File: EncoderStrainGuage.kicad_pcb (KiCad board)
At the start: 2 copper layers, 90.6 x 37.4 mm, 60 parts, among them IC1 LM60CIM3_NOPB, J1 Conn_01x05, J2 MM8130-2600RA2, J3 MM8130-2600RA2, J4 Rotary Encoder, J5 Conn_01x02_Male, J6 Conn_01x02_Male, U1 PIC16LF88-I_SO, U2 OPAMP, U3 CC2570RHAT, U4 AP3428KTTR, Y1 Crystal_GND24, Y2 Crystal

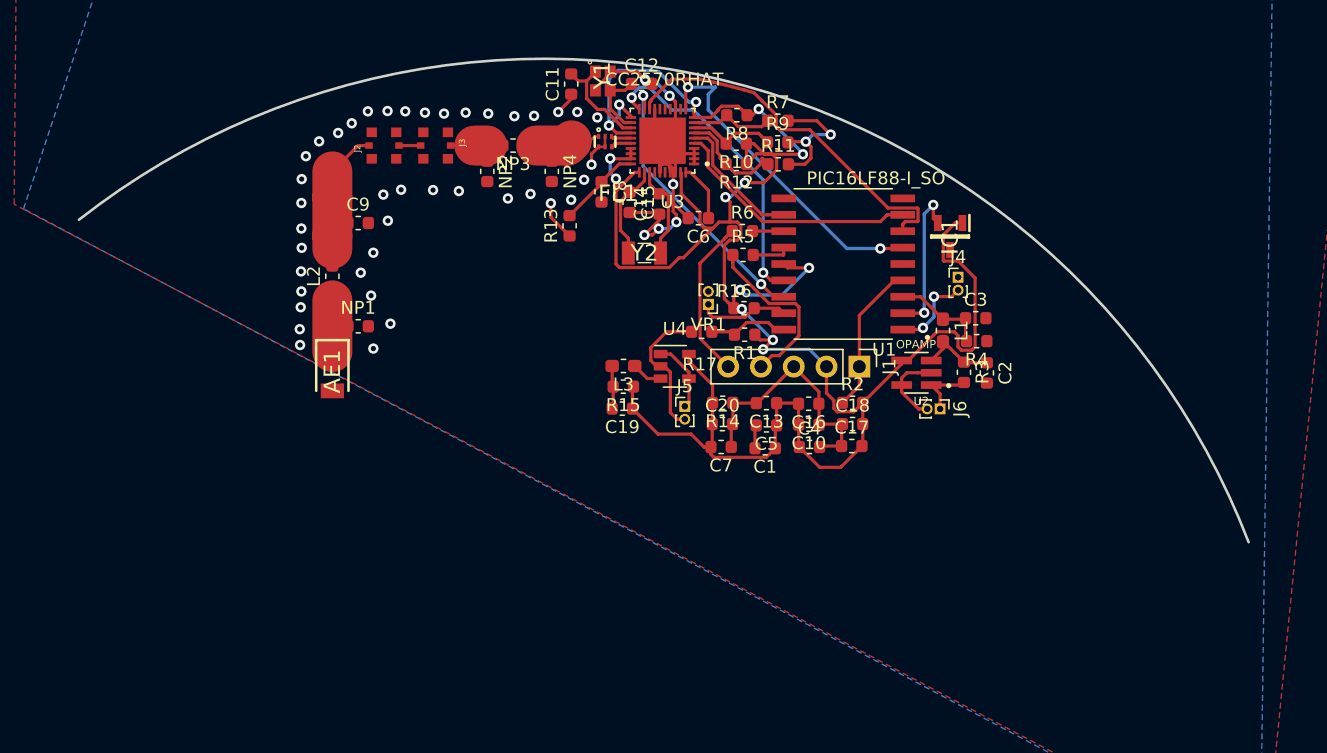
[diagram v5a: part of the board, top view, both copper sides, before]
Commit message: cleaned up a few routes
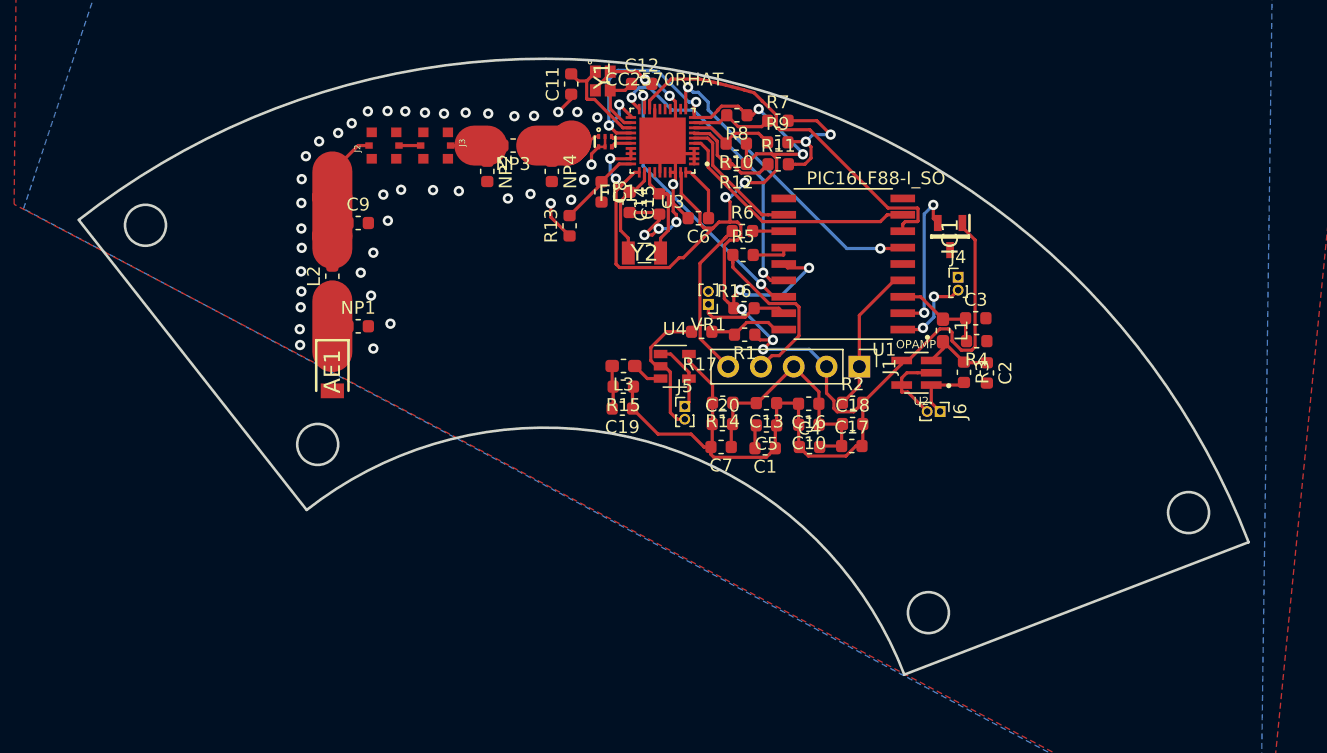
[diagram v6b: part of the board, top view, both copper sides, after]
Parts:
- moved J6 0.20 mm to (212.6, -3.40)
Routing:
- net +3V3: track 178.0 -> 172.8 mm
- net GND: track 98.8 -> 95.4 mm
- net RTS: track 25.4 -> 24.0 mm
- net Net-(R11-Pad1): track 8.51 -> 7.92 mm
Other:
- board size 90.6 x 37.4 mm -> 90.6 x 47.7 mm

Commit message: SD Card
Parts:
- added C21: 100n, Capacitor_SMD:C_0603_1608Metric, F.Cu at (157.9, 99.7)
- added C22: 100n, Capacitor_SMD:C_0603_1608Metric, F.Cu at (161.3, 95.6)
- added C23: .1uF, Capacitor_SMD:C_0603_1608Metric, F.Cu at (162.0, 98.1)
- added C24: 1uF, Capacitor_SMD:C_0603_1608Metric, F.Cu at (165.3, 95.6)
- added C25: 330P, Capacitor_SMD:C_0603_1608Metric, F.Cu at (128.7, 98.1)
- added C26: NP, Capacitor_SMD:C_0603_1608Metric, F.Cu at (132.7, 98.1)
- added C27: 330P, Capacitor_SMD:C_0603_1608Metric, F.Cu at (128.7, 100.7)
- added C28: NP, Capacitor_SMD:C_0603_1608Metric, F.Cu at (140.8, 96.2)
- added C29: 100n, Capacitor_SMD:C_0603_1608Metric, F.Cu at (132.7, 100.7)
- added C30: 1n, Capacitor_SMD:C_0603_1608Metric, F.Cu at (136.7, 98.1)
- added C31: 330P, Capacitor_SMD:C_0603_1608Metric, F.Cu at (145.6, 90.1)
- added C32: NP, Capacitor_SMD:C_0603_1608Metric, F.Cu at (140.7, 98.7)
- added J7: 47219-2001, DFFP-master:SD_472192001, F.Cu at (97.4, 94.6)
- added L4: 0, Inductor_SMD:L_0603_1608Metric_Pad1.05x0.95mm_HandSolder, F.Cu at (115.6, 89.3)
- added L5: 0, Inductor_SMD:L_0603_1608Metric_Pad1.05x0.95mm_HandSolder, F.Cu at (115.6, 91.9)
- added L6: 0, Inductor_SMD:L_0603_1608Metric_Pad1.05x0.95mm_HandSolder, F.Cu at (120.0, 89.3)
- added R1: 470, Resistor_SMD:R_0603_1608Metric, F.Cu at (145.6, 92.6)
- added R16: 470, Resistor_SMD:R_0603_1608Metric, F.Cu at (136.7, 100.7)
- added R17: 470, Resistor_SMD:R_0603_1608Metric, F.Cu at (144.8, 96.2)
- added RV1: 500 TRIM, DFFP-master:TRIM_3314J-1-202E, F.Cu at (129.7, 92.6)
- added RV2: 500 TRIM, DFFP-master:TRIM_3314J-1-202E, F.Cu at (135.8, 92.6)
- added RV3: 10k TRIM, DFFP-master:TC33X-2_1, F.Cu at (141.2, 91.7)
- added U5: INA333AIDGKR, DFFP-master:INA333AIDGKR, F.Cu at (136.1, 80.7)
- added VR2: StrainG 350 ohm, Connector_PinHeader_1.00mm:PinHeader_1x02_P1.00mm_Vertical, F.Cu at (157.6, 95.9)
- VR1: value StrainGuage -> StrainG 350 ohm
- moved AE1 147.0 mm to (119.4, 133.1)
- moved C1 147.0 mm to (152.9, 139.0)
- moved C10 147.0 mm to (156.3, 137.2)
- moved C12 147.0 mm to (143.4, 110.8)
- moved C13 147.0 mm to (153.0, 135.5)
- moved C14 147.0 mm to (144.7, 120.1)
- moved C15 147.0 mm to (142.4, 120.0)
- moved C16 147.0 mm to (156.3, 135.6)
- moved C18 147.0 mm to (159.7, 137.1)
- moved C19 147.0 mm to (141.9, 135.9)
- moved C20 147.0 mm to (149.6, 137.1)
- moved C3 147.0 mm to (169.3, 128.9)
- moved C4 147.0 mm to (156.4, 138.9)
- moved C7 147.0 mm to (149.5, 138.9)
- moved C8 147.0 mm to (140.3, 119.1)
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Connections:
- U1 pad 10: Net-(U1-Pad10) -> SCK
- U1 pad 17: Str2 -> Net-(U1-Pad17)
- VR1 pad 1: Str2 -> Str+

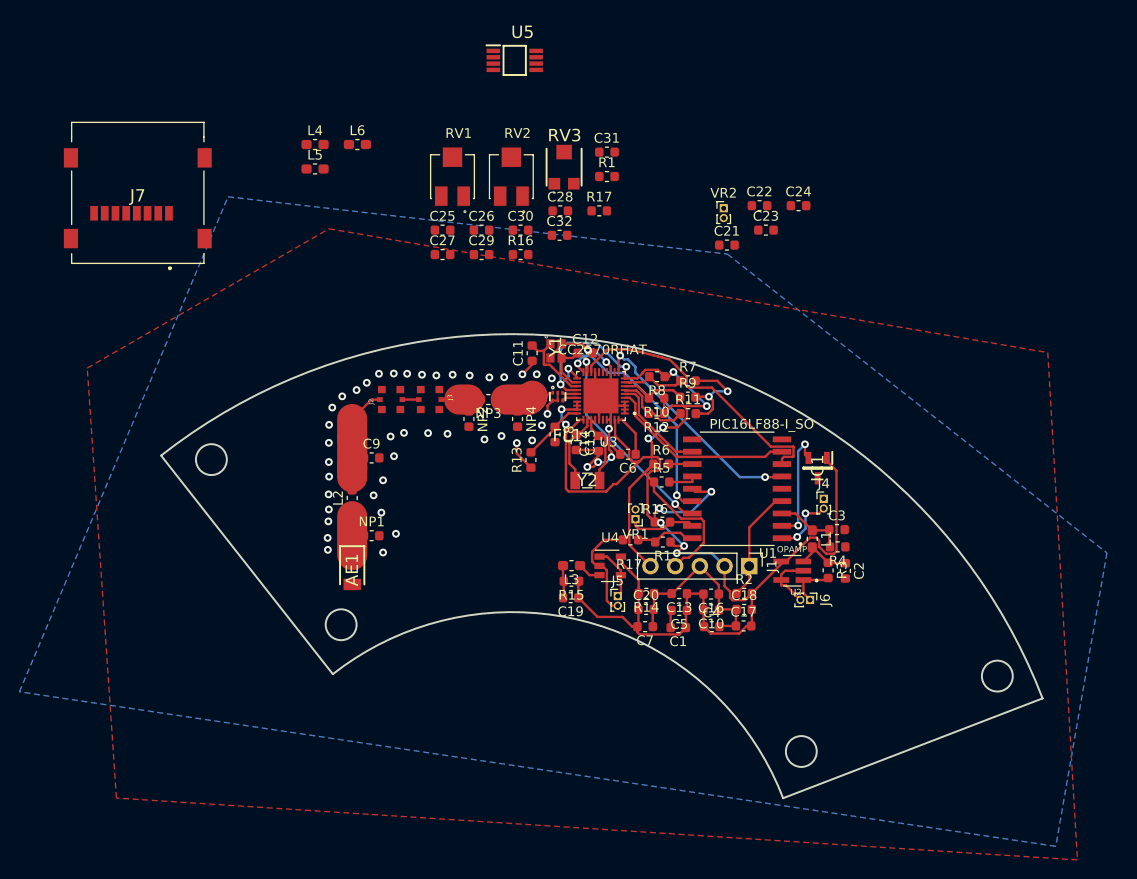
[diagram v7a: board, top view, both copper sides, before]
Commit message: "Fixed all routing"
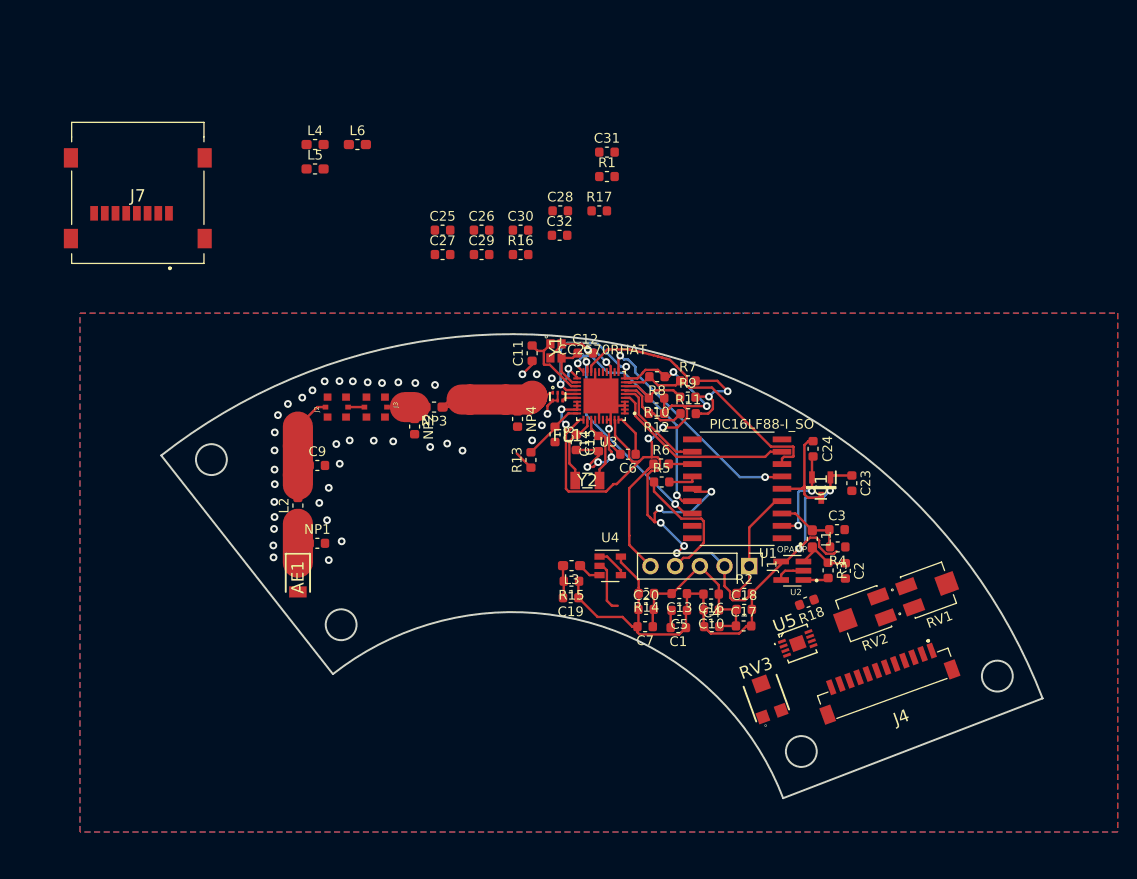
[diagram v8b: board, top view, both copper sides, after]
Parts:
- removed C21, C22: 100n, Capacitor_SMD:C_0603_1608Metric
- removed J5, J6: Conn_01x02_Male, Connector_PinHeader_1.00mm:PinHeader_1x02_P1.00mm_Vertical
- removed the R1 at (151.4, 130.2)
- removed the R16 at (151.3, 128.2)
- removed the R17 at (148.0, 130.0)
- removed VR1, VR2: StrainG 350 ohm, Connector_PinHeader_1.00mm:PinHeader_1x02_P1.00mm_Vertical
- added R18: 200k, Resistor_SMD:R_0603_1608Metric, F.Cu at (166.2, 136.4)
- J4: value Rotary Encoder -> Conn_01x12; footprint Connector_PinHeader_1.00mm:PinHeader_1x02_P1.00mm_Vertical -> DFFP-master:1-1734595-2
- U5: value INA333AIDGKR -> MCP6N11T; footprint DFFP-master:INA333AIDGKR -> DFFP-master:MCP6N11T-010E
- moved U5 66.6 mm to (165.2, 140.6), turned to 20 degrees
- moved RV1 64.8 mm to (178.7, 135.2), turned to 290 degrees
- moved RV3 58.4 mm to (162.0, 146.3), turned to 20 degrees
- moved RV2 57.7 mm to (172.0, 137.6), turned to 110 degrees
- moved C23 27.5 mm to (170.8, 124.2), turned to 270 degrees
- moved C24 25.0 mm to (166.8, 120.6), turned to 90 degrees
- moved J4 20.0 mm to (180.7, 141.1), turned to 200 degrees
- moved AE1 5.64 mm to (113.8, 133.8)
- moved J3 5.64 mm to (121.8, 116.3)
- moved L2 5.64 mm to (113.8, 126.5)
- moved NP3 5.64 mm to (127.8, 116.3)
- moved C9 5.64 mm to (115.8, 122.3)
- moved J2 5.64 mm to (117.8, 116.3)
- moved NP1 5.64 mm to (115.8, 130.3)
- moved NP2 5.64 mm to (125.8, 118.3)
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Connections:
- C1 pad 1: +3V3 -> Str2_3v3
- C1 pad 2: GND -> Str1_Gnd
- C10 pad 1: GND -> Str1_Gnd
- C10 pad 2: +3V3 -> Str2_3v3
- C11 pad 1: GND -> Str1_Gnd
- C12 pad 2: GND -> Str1_Gnd
- C13 pad 1: +3V3 -> Str2_3v3
- C13 pad 2: GND -> Str1_Gnd
- C14 pad 1: GND -> Str1_Gnd
- C15 pad 2: GND -> Str1_Gnd
- C16 pad 1: GND -> Str1_Gnd
- C16 pad 2: +3V3 -> Str2_3v3
- C17 pad 1: GND -> Str1_Gnd
- C17 pad 2: +3V3 -> Str2_3v3
- C18 pad 1: GND -> Str1_Gnd
- C18 pad 2: +3V3 -> Str2_3v3
- C19 pad 1: +3V3 -> Str2_3v3
- C2 pad 2: GND -> Str1_Gnd
- C20 pad 1: +3V3 -> Str2_3v3
- C20 pad 2: GND -> Str1_Gnd
- C23 pad 1: +3V3 -> Str2_3v3
- C23 pad 2: GND -> Str1_Gnd
- C24 pad 2: GND -> Str1_Gnd
- C25 pad 2: GND -> Str1_Gnd
- C26 pad 2: GND -> Str1_Gnd
- C27 pad 2: GND -> Str1_Gnd
- C28 pad 2: GND -> Str1_Gnd
- C29 pad 1: +3V3 -> Str2_3v3
- C29 pad 2: GND -> Str1_Gnd
- C3 pad 2: GND -> Str1_Gnd
- C30 pad 1: +3V3 -> Str2_3v3
- C30 pad 2: GND -> Str1_Gnd
- C31 pad 2: GND -> Str1_Gnd
- C32 pad 2: GND -> Str1_Gnd
- C4 pad 1: +3V3 -> Str2_3v3
- C4 pad 2: GND -> Str1_Gnd
- C5 pad 1: +3V3 -> Str2_3v3
- C5 pad 2: GND -> Str1_Gnd
- C6 pad 2: GND -> Str1_Gnd
- C7 pad 1: GND -> Str1_Gnd
- C7 pad 2: +3V3 -> Str2_3v3
- C8 pad 2: GND -> Str1_Gnd
- C9 pad 2: GND -> Str1_Gnd
- FL1 pad 2: GND -> Str1_Gnd
- FL1 pad 5: GND -> Str1_Gnd
- FL1 pad 6: GND -> Str1_Gnd
- IC1 pad 1: +3V3 -> Str2_3v3
- IC1 pad 3: GND -> Str1_Gnd
- J1 pad 2: +3V3 -> Str2_3v3
- J1 pad 3: GND -> Str1_Gnd
- J2 pad GND1: GND -> Str1_Gnd
- J2 pad GND2: GND -> Str1_Gnd
- J2 pad GND3: GND -> Str1_Gnd
- J2 pad GND4: GND -> Str1_Gnd
- J3 pad GND1: GND -> Str1_Gnd
- J3 pad GND2: GND -> Str1_Gnd
- J3 pad GND3: GND -> Str1_Gnd
- J3 pad GND4: GND -> Str1_Gnd
- J4 pad 1: GND -> SSTB
- J4 pad 2: PotOut -> Str2_3v3
- J7 pad 10: GND -> Str1_Gnd
- J7 pad 11: GND -> Str1_Gnd
- J7 pad 12: GND -> Str1_Gnd
- J7 pad 4: +3V3 -> Str2_3v3
- J7 pad 6: GND -> Str1_Gnd
- J7 pad 9: GND -> Str1_Gnd
- NP1 pad 2: GND -> Str1_Gnd
- NP2 pad 2: GND -> Str1_Gnd
- NP4 pad 2: GND -> Str1_Gnd
- R10 pad 1: +3V3 -> Str2_3v3
- R11 pad 2: GND -> Str1_Gnd
- R12 pad 1: +3V3 -> Str2_3v3
- R13 pad 1: GND -> Str1_Gnd
- R14 pad 1: GND -> Str1_Gnd
- R14 pad 2: +3V3 -> Str2_3v3
- R15 pad 1: +3V3 -> Str2_3v3
- R2 pad 2: +3V3 -> Str2_3v3
- R3 pad 2: Net-(J6-Pad1) -> PSout
- R4 pad 1: GND -> Str1_Gnd
- R7 pad 2: GND -> Str1_Gnd
- R8 pad 1: +3V3 -> Str2_3v3
- R9 pad 2: GND -> Str1_Gnd
- RV1 pad 1: GND -> Str1_Gnd
- RV2 pad 3: +3V3 -> Str2_3v3
- RV3 pad 1: Net-(RV3-Pad1) -> Str1_Gnd
- RV3 pad 3: Net-(RV3-Pad3) -> Net-(R18-Pad2)
- U1 pad 14: +3V3 -> Str2_3v3
- U1 pad 17: Net-(U1-Pad17) -> SSTB
- U1 pad 5: GND -> Str1_Gnd
- U1 pad 7: Sleep -> MOSI
- U1 pad 9: Net-(U1-Pad9) -> Sleep
- U2 pad 1: Net-(J6-Pad1) -> PSout
- U2 pad 2: GND -> Str1_Gnd
- U2 pad 4: +3V3 -> Str2_3v3
- U2 pad 5: GND -> Str1_Gnd
- U3 pad 1: GND -> Str1_Gnd
- U3 pad 10: +3V3 -> Str2_3v3
- U3 pad 13: GND -> Str1_Gnd
- U3 pad 17: GND -> Str1_Gnd
- U3 pad 2: GND -> Str1_Gnd
- U3 pad 21: +3V3 -> Str2_3v3
- U3 pad 24: +3V3 -> Str2_3v3
- U3 pad 27: +3V3 -> Str2_3v3
- U3 pad 28: +3V3 -> Str2_3v3
- U3 pad 29: +3V3 -> Str2_3v3
- U3 pad 3: GND -> Str1_Gnd
- U3 pad 31: +3V3 -> Str2_3v3
- U3 pad 35: GND -> Str1_Gnd
- U3 pad 37: GND -> Str1_Gnd
- U3 pad 38: GND -> Str1_Gnd
- U3 pad 39: +3V3 -> Str2_3v3
- U3 pad 4: GND -> Str1_Gnd
- U3 pad 41: GND -> Str1_Gnd
- U4 pad 2: GND -> Str1_Gnd
- U4 pad 5: +3V3 -> Str2_3v3
- U5 pad 1: Net-(RV3-Pad1) -> Net-(R18-Pad2)
- U5 pad 2: Str+ -> Str-
- U5 pad 3: Str- -> Str+
- U5 pad 4: GND -> Str1_Gnd
- U5 pad 5: GND -> Str1_Gnd
- U5 pad 7: +3V3 -> Str2_3v3
- U5 pad 8: Net-(RV3-Pad3) -> Str2_3v3
- Y1 pad 2: GND -> Str1_Gnd
- Y1 pad 4: GND -> Str1_Gnd
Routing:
- net Str2_3v3: track 0.00 -> 173.2 mm, vias 0 -> 16
- net +3V3: track 172.8 -> 0.00 mm, vias 14 -> 0
- net Str1_Gnd: track 0.00 -> 96.2 mm, vias 0 -> 11
- net GND: track 95.4 -> 0.11 mm, vias 49 -> 37
- net Net-(FL1-Pad1): track 7.80 -> 15.1 mm
- net Str2: track 7.10 -> 0.00 mm
- net PotOut: track 6.48 -> 0.00 mm, vias 2 -> 0
- net Str1: track 6.28 -> 0.66 mm
- net Net-(J6-Pad1): track 4.95 -> 0.00 mm
- net PSout: track 7.42 -> 10.0 mm
- net Vin: track 5.55 -> 3.27 mm
- net TempOut: track 11.9 -> 10.1 mm
- added copper zone on B.Cu, net Str1_Gnd
- added copper zone on F.Cu, net Str1_Gnd
- removed copper zone on B.Cu, net GND
- removed copper zone on F.Cu, net GND
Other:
- outline, holes or cut-outs redrawn
